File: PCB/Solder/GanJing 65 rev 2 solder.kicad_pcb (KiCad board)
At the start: 2 copper layers, 323.9 x 95.2 mm, 150 parts, among them SW1 EC11_rotary_encoder, U1 Elite-C

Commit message: finished firmware
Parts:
- removed the D58 at (309.6, 131.0)
- moved D43 32.4 mm to (309.6, 131.0)
- renumbered D59 to D58, D60 to D59, D61 to D60, D62 to D61, D63 to D62, D64 to D63, D65 to D64, D66 to D65, D67 to D66, D68 to D67, D69 to D68, D70 to D69, D71 to D70, MX59 to MX58, MX60 to MX59, MX61 to MX60, MX62 to MX61, MX63 to MX62, MX64 to MX63, MX65 to MX64, MX66 to MX65, MX67 to MX66, MX68 to MX67, MX69 to MX68, MX70 to MX69, MX71 to MX70, MX72 to MX71, MX73 to MX72, MX74 to MX73, MX75 to MX74, MX58 to MX75
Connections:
- MX75 pad 2: Net-(D58-Pad2) (its old number) -> Net-(D43-Pad2)
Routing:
- net row_4: track 400.9 -> 365.5 mm
- net Net-(D43-Pad2): track 34.8 -> 19.4 mm
- net Net-(D58-Pad2) (its old number): track 11.6 -> 0.00 mm
- net row_3: track 367.0 -> 365.6 mm
- net GND: vias 100 -> 102

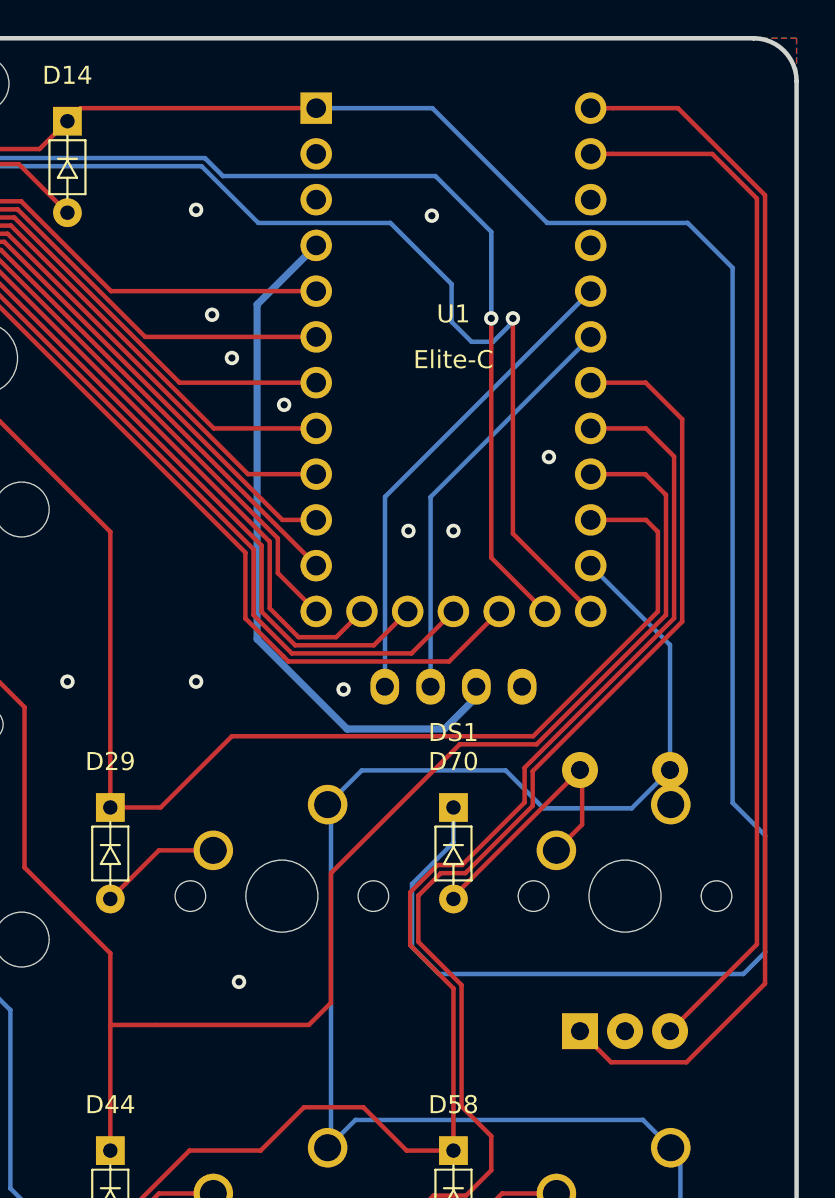
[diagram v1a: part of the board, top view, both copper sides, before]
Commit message: Updated PCBs to adjust the location of the encoder plus fix routing errors in the hotswap version. Plate file is also completed, case files still need to be finalized
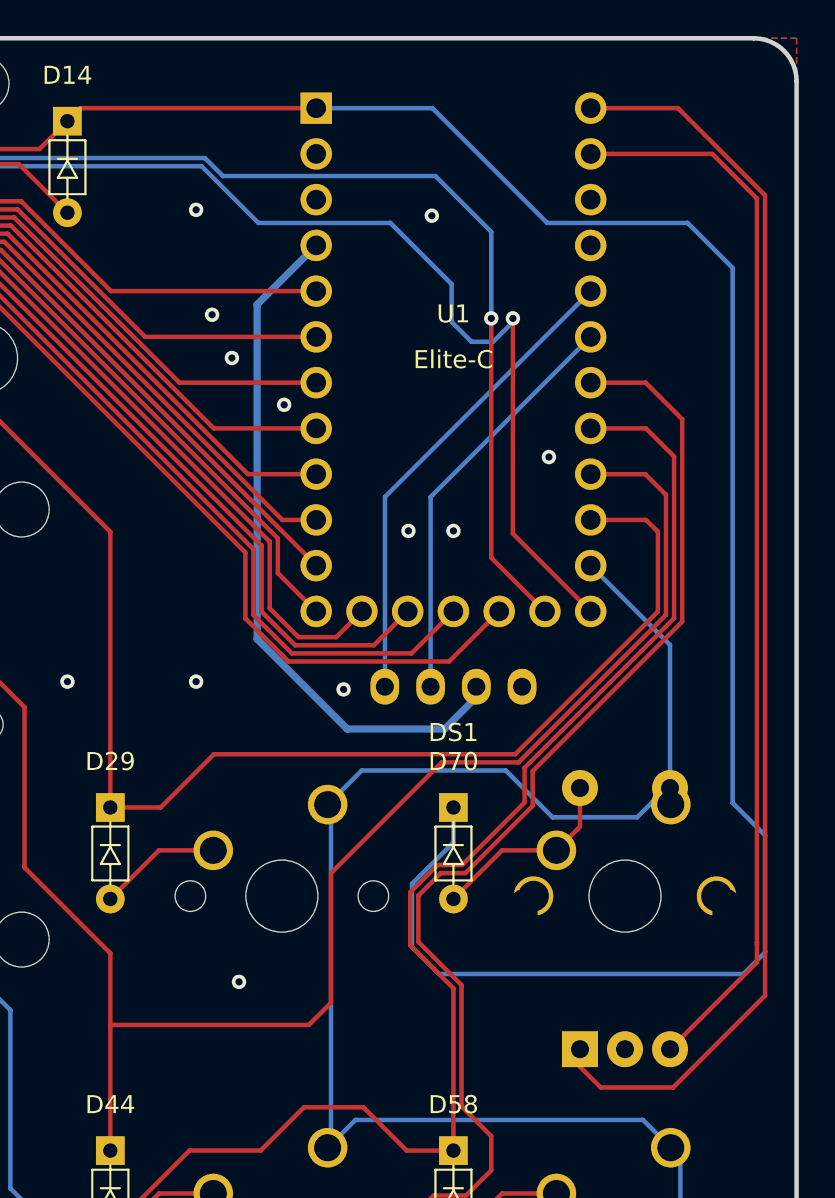
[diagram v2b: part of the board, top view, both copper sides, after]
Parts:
- removed SW1: EC11_rotary_encoder, GanJing_components:EC11_rotary_encoder
- added SWe: EC11_rotary_encoder, GanJing_components:EC11_rotary_encoder, F.Cu at (364.3, 143.9)
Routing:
- net S2: track 15.2 -> 11.0 mm
- net rotory_1: track 68.3 -> 70.0 mm
- net rotory_2: track 58.5 -> 59.6 mm

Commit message: Switching to KiCad 6.0.1 so some files have been converted and the component symbol library files has been converted from .lib to .kicad_sym
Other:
- board size 323.9 x 95.2 mm -> 323.8 x 95.2 mm
- net class Default removed
